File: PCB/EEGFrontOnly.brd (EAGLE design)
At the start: 160 x 100 mm, 36 parts, among them IC1 ADS1299-X, J2 USB_B_PTH, U1 LP2985-33DBVT, U2 B0505S-1WB0505S-1W, U3 TPS60403DBVT, U4 TPS73225DBVR, U5 TPS73225DBVR

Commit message: ads stuff init
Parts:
- added C21, C23, C25, C30, C31, C32, C34: 1.0uF, SparkFun-Capacitors:0402
- added C22, C24, C26, C27, C33, C35: 0.1uF, SparkFun-Capacitors:0402
- added C28: 10uF, SparkFun-Capacitors:0402
- added C29: 100uF, jingjieparts:1210
- added C36, C37: NI, SparkFun-Capacitors:0402
- added J5: (no value), SparkFun-Connectors:1X02
- moved IC1 94.8 mm to (47.9, 64.1)
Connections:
- new net N$10: C27.2, C28.2, IC1.24
- new net N$11: IC1.18, J5.1
- new net N$12: IC1.17, J5.2
- new net VCAP1: C29.1, IC1.28
- new net VCAP2: C30.1, IC1.30
- new net VCAP3: C31.1, C33.1, IC1.55
- new net VCAP4: C32.2, IC1.26
- net AGND: now also C21.2, C22.2, C23.2, C24.2, C25.2, C26.2, C34.2, C35.2
- net AVDD: now also C21.1, C22.1, C36.1, C37.1, IC1.19, IC1.21, IC1.22, IC1.54, IC1.56, IC1.59
- net AVSS: now also C23.1, C24.1, C27.1, C28.1, C29.2, C30.2, C31.2, C32.1, C33.2, C34.1, C35.1, C36.2, C37.2, IC1.20, IC1.23, IC1.25, IC1.32, IC1.53, IC1.57, IC1.58
- net DGND: now also IC1.33, IC1.49, IC1.51
- net DVDD: now also C25.1, C26.1, IC1.48, IC1.50
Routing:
- net AVSS: track 2.20 -> 28.6 mm
- net AVDD: track 2.13 -> 14.0 mm
- net VCAP2: track 0.00 -> 5.69 mm
- net N$10: track 0.00 -> 4.90 mm
- net VCAP1: track 0.00 -> 4.27 mm
- net VCAP4: track 0.00 -> 3.71 mm
- net AGND: track 47.4 -> 48.8 mm

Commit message: STUFF
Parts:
- added C38: 1.5nF, SparkFun-Capacitors:0402
- added C39, C40, C41, C42, C43, C44, C45, C46, C47, C48: 4.7nF, SparkFun-Capacitors:0402
- added R10, R11, R12, R13, R4, R5, R6, R7, R8, R9: 4.99K, SparkFun-Resistors:0402
- added R3: 1M, SparkFun-Resistors:0402
- added U6, U7, U8: TPD4E1B06DCKR, jingjieparts:SC70-6
- moved J5 77.8 mm to (38.1, 49.4), turned to 90 degrees
- moved C21 0.77 mm to (44.5, 77.2)
- moved C22 0.77 mm to (44.5, 75.8)
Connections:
- new net N$13: C38.2, IC1.61, R3.1
- new net N$14: C38.1, C39.1, IC1.62, IC1.63, R3.2, R4.2
- new net N$15: C40.1, IC1.2, R5.2
- new net N$16: C41.1, IC1.4, R6.2
- new net N$17: C42.1, IC1.6, R7.2
- new net N$18: C43.1, IC1.8, R8.2
- new net N$19: C44.1, IC1.10, R9.2
- new net N$20: C45.1, IC1.12, R10.2
- new net N$21: C46.1, IC1.14, R11.2
- new net N$22: C47.1, IC1.16, R12.2
- new net P_BIAS: R4.1, U6.1
- new net P_IN1: R12.1, U8.1
- new net P_IN2: R11.1, U7.4
- new net P_IN3: R10.1, U7.5
- new net P_IN4: R9.1, U7.2
- new net P_IN5: R8.1, U7.1
- new net P_IN6: R7.1, U6.4
- new net P_IN7: R6.1, U6.5
- new net P_IN8: R5.1, U6.2
- new net P_REF: R13.1, U8.2
- net AGND: now also C39.2, C40.2, C41.2, C42.2, C43.2, C44.2, C45.2, C46.2, C47.2, C48.2, U6.3, U7.3, U8.3
- net DGND: now also IC1.31
- net N$12: now also C48.1, R13.2
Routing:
- net N$12: track 0.00 -> 23.4 mm
- net N$22: track 0.00 -> 18.2 mm
- net N$21: track 0.00 -> 17.3 mm
- net N$15: track 0.00 -> 17.2 mm
- net N$16: track 0.00 -> 16.2 mm
- net N$20: track 0.00 -> 16.2 mm
- net N$19: track 0.00 -> 15.4 mm
- net N$17: track 0.00 -> 15.3 mm
- net N$18: track 0.00 -> 14.4 mm
- net N$11: track 0.00 -> 13.0 mm
- net P_BIAS: track 0.00 -> 7.64 mm
- net P_IN5: track 0.00 -> 7.22 mm
- net P_IN8: track 0.00 -> 6.55 mm
- net AGND: track 48.8 -> 55.4 mm
- net P_IN2: track 0.00 -> 6.20 mm
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
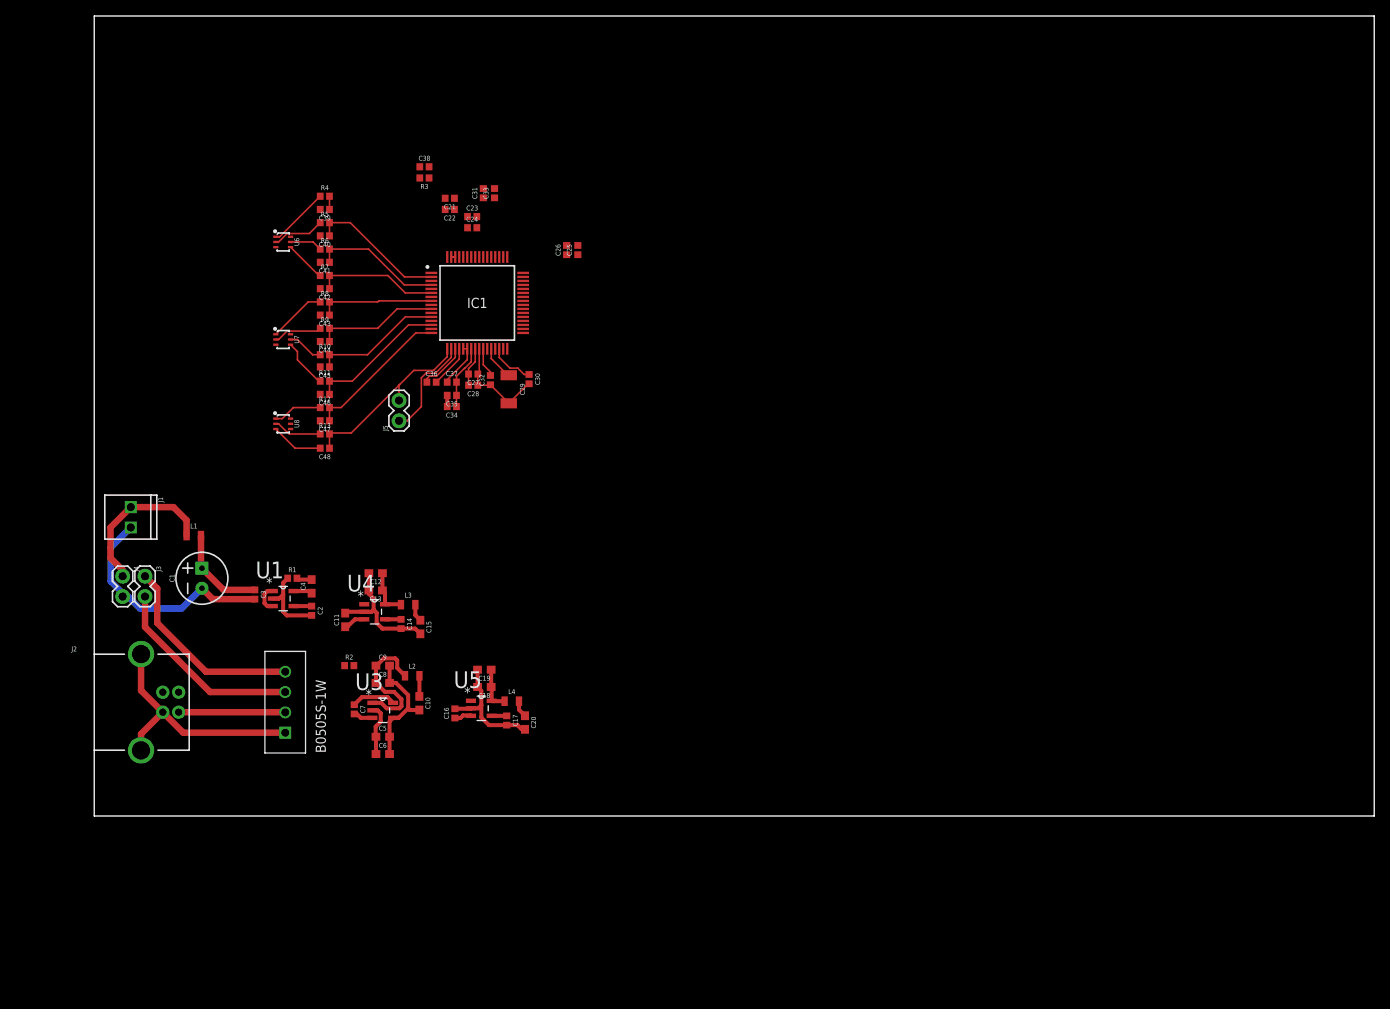
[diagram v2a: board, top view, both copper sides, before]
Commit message: partly complete the ADS part
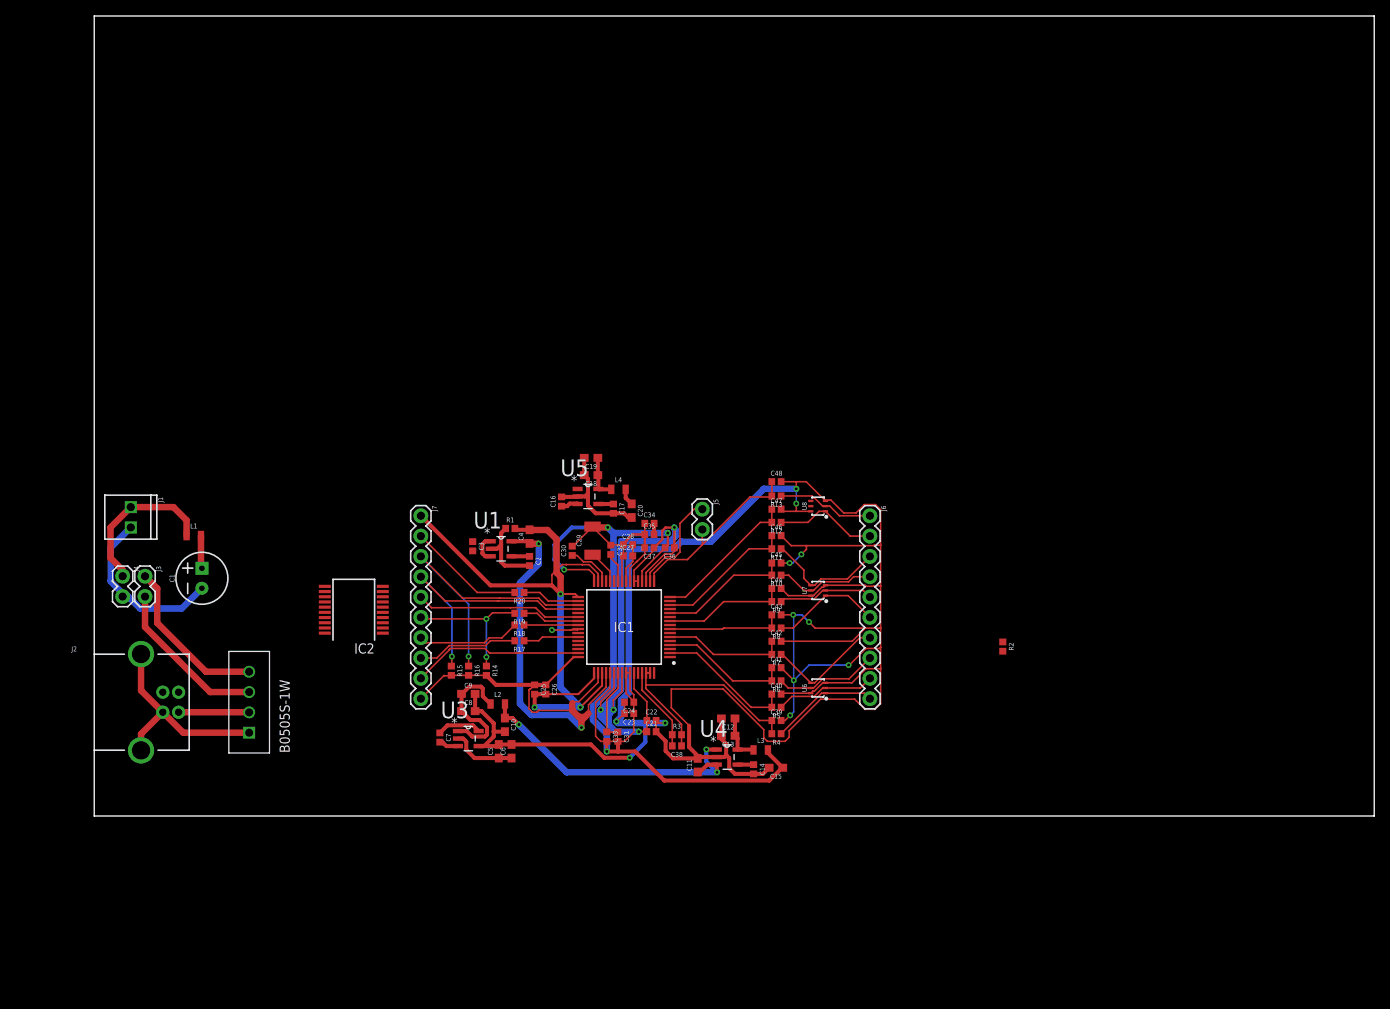
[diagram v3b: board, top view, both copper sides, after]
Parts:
- added IC2: ADUM3151-3, analog-devices-adum315x:SSOP20
- added J6, J7: (no value), SparkFun-Connectors:1X10
- added R14, R15, R16: 10k, SparkFun-Resistors:0402
- added R17, R18, R19, R20: 22, SparkFun-Resistors:0402
- moved R4 87.8 mm to (85.3, 10.3), turned to 180 degrees
- moved U6 87.1 mm to (90.5, 16.0), turned to 90 degrees
- moved C39 85.2 mm to (85.3, 11.9), turned to 0 degrees
- moved R5 82.8 mm to (85.3, 13.6), turned to 180 degrees
- moved R2 81.7 mm to (113.6, 21.2), turned to 270 degrees
- moved C40 80.4 mm to (85.3, 15.2), turned to 0 degrees
- moved C38 79.0 mm to (72.8, 8.76), turned to 180 degrees
- moved R6 78.1 mm to (85.3, 16.9), turned to 180 degrees
- moved R3 76.4 mm to (72.8, 10.2), turned to 0 degrees
- moved C41 75.9 mm to (85.3, 18.5), turned to 0 degrees
- moved U7 73.9 mm to (90.5, 28.2), turned to 90 degrees
- moved R7 73.7 mm to (85.3, 20.2), turned to 180 degrees
- moved C42 71.6 mm to (85.3, 21.8), turned to 0 degrees
- moved C21 71.3 mm to (69.7, 10.5), turned to 0 degrees
- moved C31 70.0 mm to (65.5, 9.91), turned to 270 degrees
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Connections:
- new net CLK_NC: IC1.37
- new net GND1: IC2.2, IC2.3
- new net GND2: IC2.11, IC2.12
- new net N$23: IC1.43, R17.1
- new net N$24: IC1.40, R18.1
- new net N$25: IC1.39, R19.1
- new net N$26: IC1.34, R20.1
- new net PWD: IC1.35, J7.3, R16.1
- new net RST: IC1.36, J7.4, R15.1
- new net SPI_CLK: J7.7, R18.2
- new net SPI_CS: J7.6, R14.1, R19.2
- new net SPI_DRDY: IC1.47, J7.9
- new net SPI_MISO: J7.8, R17.2
- new net SPI_MOSI: J7.2, R20.2
- new net SPI_START: IC1.38, J7.5
- new net VDD1: IC2.1
- new net VDD2: IC2.20
- net AGND: now also U6.6, U7.6, U8.6; no longer C25.2, C26.2
- net DGND: now also C25.2, C26.2, IC1.41, J7.1
- net DVDD: now also IC1.52, J7.10, R14.2, R15.2, R16.2
- net P_BIAS: now also J6.10
- net P_IN1: now also J6.2
- net P_IN2: now also J6.3
- net P_IN3: now also J6.4
- net P_IN4: now also J6.5
- net P_IN5: now also J6.6
- net P_IN6: now also J6.7
- net P_IN7: now also J6.8
- net P_IN8: now also J6.9
- net P_REF: now also J6.1
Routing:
- net AGND: track 55.4 -> 321.0 mm, vias 0 -> 12
- net AVSS: track 28.6 -> 142.4 mm, vias 0 -> 4
- net DGND: track 1.90 -> 87.0 mm, vias 0 -> 4
- net DVDD: track 2.52 -> 81.9 mm, vias 0 -> 2
- net AVDD: track 14.0 -> 83.3 mm, vias 0 -> 4
- net PWD: track 0.00 -> 38.4 mm, vias 0 -> 1
- net RST: track 0.00 -> 34.2 mm, vias 0 -> 1
- net NVCC: track 5.35 -> 39.6 mm, vias 0 -> 3
- net N$14: track 2.15 -> 30.7 mm
- net SPI_DRDY: track 0.00 -> 21.5 mm
- net SPI_START: track 0.00 -> 20.7 mm
- net SPI_CS: track 0.00 -> 18.1 mm, vias 0 -> 2
- net SPI_MOSI: track 0.00 -> 14.7 mm
- net SPI_CLK: track 0.00 -> 12.9 mm
- net SPI_MISO: track 0.00 -> 12.6 mm
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
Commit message: SPI_ISO
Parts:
- added C49, C50: 10uF, SparkFun-Capacitors:0603
- added C51, C52: 22nF, SparkFun-Capacitors:0402
- added IC3: HT7333, holtek2:SOT-89
- added J8: (no value), SparkFun-Connectors:1X10
- moved C15 106.9 mm to (16.0, 87.6), turned to 0 degrees
- moved C14 103.7 mm to (18.8, 87.7), turned to 90 degrees
- moved L3 101.1 mm to (17.9, 85.3), turned to 180 degrees
- moved U6 100.8 mm to (10.7, 77.6), turned to 270 degrees
- moved R4 100.7 mm to (15.9, 83.3), turned to 0 degrees
- moved C39 98.3 mm to (15.9, 81.7), turned to 180 degrees
- moved U4 97.3 mm to (22.1, 86.2), turned to 180 degrees
- moved R5 96.0 mm to (15.9, 80.0), turned to 0 degrees
- moved C11 94.9 mm to (25.8, 87.2), turned to 270 degrees
- moved J6 94.5 mm to (4.25, 56.1), turned to 90 degrees
- moved C40 93.8 mm to (15.9, 78.4), turned to 180 degrees
- moved C13 93.2 mm to (22.0, 83.6), turned to 0 degrees
- moved R6 91.6 mm to (15.9, 76.7), turned to 0 degrees
- moved C12 89.8 mm to (22.0, 81.4), turned to 0 degrees
- moved C41 89.4 mm to (15.9, 75.0), turned to 180 degrees
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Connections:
- removed net GND1: IC2.2, IC2.3
- removed net GND2: IC2.11, IC2.12
- removed net VDD1: IC2.1
- removed net VDD2: IC2.20
- new net SPI_ISO_CLK: IC2.3, J8.9
- new net SPI_ISO_CS: IC2.6, J8.6
- new net SPI_ISO_DRDY: IC2.9, J8.3
- new net SPI_ISO_MISO: IC2.5, J8.7
- new net SPI_ISO_MOSI: IC2.4, J8.8
- new net SPI_ISO_RST: IC2.8, J8.4
- new net SPI_ISO_START: IC2.7, J8.5
- new net SPI_PWD: J8.2
- new net VCCIO: C50.1, C51.1, IC2.1, IC3.1, J8.10
- net DGND: now also C52.2, IC2.11, IC2.19
- net DVDD: now also C52.1, IC2.20
- net GND-ISO: now also C49.2, C50.2, C51.2, IC2.10, IC2.2, IC3.2, J8.1
- net RST: now also IC2.13
- net SPI_CLK: now also IC2.18
- net SPI_CS: now also IC2.15
- net SPI_DRDY: now also IC2.12
- net SPI_MISO: now also IC2.16
- net SPI_MOSI: now also IC2.17
- net SPI_START: now also IC2.14
- net VCC-ISO: now also C49.1, IC3.3, IC3.4
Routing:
- net GND-ISO: track 26.1 -> 67.6 mm
- net VCCIO: track 0.00 -> 19.8 mm
- net DVDD: track 81.9 -> 101.5 mm
- net SPI_CLK: track 12.9 -> 28.8 mm, vias 0 -> 1
- net SPI_ISO_CLK: track 0.00 -> 11.3 mm
- net SPI_MOSI: track 14.7 -> 25.1 mm, vias 0 -> 1
- net DGND: track 87.0 -> 97.4 mm
- net RST: track 34.2 -> 44.2 mm, vias 1 -> 2
- net SPI_MISO: track 12.6 -> 22.5 mm, vias 0 -> 1
- net SPI_ISO_MOSI: track 0.00 -> 9.51 mm
- net SPI_DRDY: track 21.5 -> 30.9 mm
- net SPI_ISO_DRDY: track 0.00 -> 8.60 mm
- net SPI_ISO_MISO: track 0.00 -> 7.98 mm
- net SPI_ISO_RST: track 0.00 -> 7.81 mm
- net SPI_ISO_CS: track 0.00 -> 7.20 mm
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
